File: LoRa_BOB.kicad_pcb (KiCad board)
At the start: 4 copper layers, 23 x 77 mm, 6 parts, among them U1 RFM95W-915S2

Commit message: Minor advances
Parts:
- removed the A1 at (174.2, 162.9)
- added C3: 0.1uF, Capacitor_SMD:C_0805_2012Metric_Pad1.18x1.45mm_HandSolder, F.Cu at (255.6, 172.8)
- added U1: XC6210B332MR-G, Package_TO_SOT_SMD:SOT-23-5, F.Cu at (261.1, 168.0)
- added U3: 74HC4050D, Package_SO:SOIC-16_3.9x9.9mm_P1.27mm, F.Cu at (255.7, 179.1)
- C1, C2: value C -> 10uF; footprint Capacitor_SMD:C_0805_2012Metric_Pad1.18x1.45mm_HandSolder -> Capacitor_SMD:C_1206_3216Metric_Pad1.33x1.80mm_HandSolder
- moved C1 40.6 mm to (264.7, 168.2)
- moved C2 36.3 mm to (255.6, 168.8)
- renumbered A2 to A1, U1 to U2
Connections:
- A1 pad 11: unconnected-(A2-SCK/D24-Pad11) -> /SCK
- A1 pad 12: unconnected-(A2-MOSI/D23-Pad12) -> /MOSI
- A1 pad 13: unconnected-(A2-MISO/D22-Pad13) -> /MISO
- A1 pad 16: unconnected-(A2-DIO1-Pad16) -> Net-(A1-DIO1)
- A1 pad 2: Net-(A2-3V3) -> Net-(A1-3V3)
- A1 pad 26: unconnected-(A2-USB-Pad26) -> Net-(A1-USB)
- A1 pad 6: unconnected-(A2-A1-Pad6) -> /~{RESET}
- A1 pad 7: Net-(A2-A2) -> /CS
- A1 pad 9: Net-(A2-A4) -> Net-(A1-A4)
- C1 pad 1: Net-(A2-3V3) -> Net-(A1-USB)
- C1 pad 2: GND -> Net-(U1-GND)
- C2 pad 1: Net-(A2-3V3) -> +3V3
- C2 pad 2: GND -> Net-(U1-GND)
- U2 pad 13: Net-(A2-3V3) -> +3V3
- U2 pad 15: unconnected-(U1-DIO1-Pad15) -> Net-(A1-DIO1)
- U2 pad 2: unconnected-(U1-MISO-Pad2) -> /MISO
- U2 pad 3: unconnected-(U1-MOSI-Pad3) -> /MOSI_3V
- U2 pad 4: unconnected-(U1-SCK-Pad4) -> /SCK_3V
- U2 pad 5: Net-(A2-A2) -> /CS_3V
- U2 pad 6: Net-(A2-A4) -> Net-(U2-RESET)

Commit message: Routed but could be better
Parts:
- moved C3 31.7 mm to (254.2, 204.5)
- moved AE1 2.56 mm to (257.2, 221.1)
- moved U1 2.07 mm to (259.1, 167.6)
- moved C2 2.01 mm to (254.0, 167.6)
- moved U3 2.00 mm to (257.1, 177.7)
- moved U2 1.41 mm to (256.6, 192.9)
- moved A1 1.19 mm to (246.4, 162.5)
- moved C1 0.76 mm to (264.2, 167.6)
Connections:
- A1 pad 2: Net-(A1-3V3) -> unconnected-(A1-3V3-Pad2)
- C1 pad 2: Net-(U1-GND) -> GND
- C2 pad 2: Net-(U1-GND) -> GND
- C3 pad 2: Net-(U1-GND) -> GND
- U1 pad 2: Net-(U1-GND) -> GND
- U3 pad 1: Net-(A1-3V3) -> +3V3
- U3 pad 8: unconnected-(U3-GND-Pad8) -> GND
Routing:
- net /MOSI: track 0.00 -> 23.6 mm, vias 0 -> 1
- net Net-(A1-A5): track 0.00 -> 20.8 mm
- net Net-(A1-USB): track 0.00 -> 20.6 mm, vias 0 -> 2
- net /CS_3V: track 0.00 -> 20.5 mm
- net Net-(A1-DIO1): track 0.00 -> 19.6 mm, vias 0 -> 2
- net /MISO: track 0.00 -> 19.2 mm, vias 0 -> 2
- net /SCK: track 0.00 -> 13.7 mm, vias 0 -> 1
- net +3V3: track 0.00 -> 13.6 mm, vias 0 -> 4
- net /CS: track 0.00 -> 12.9 mm
- net GND: track 0.00 -> 12.3 mm, vias 0 -> 5
- net /MOSI_3V: track 0.00 -> 10.9 mm, vias 0 -> 2
- net Net-(A1-A4): track 0.00 -> 7.42 mm
- net /SCK_3V: track 0.00 -> 5.64 mm, vias 0 -> 2
- net Net-(U2-RESET): track 0.00 -> 5.35 mm
- net Net-(AE1-A): track 11.7 -> 15.2 mm
- added copper zone on In2.Cu, net +3V3
- added copper zone on B.Cu, net GND
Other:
- board size 23 x 77 mm -> 22.9 x 77.5 mm

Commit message: New Template
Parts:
- removed A1: Adafruit_Feather_M0_RFM9x_LoRa_Radio, Module:Adafruit_Feather_M0_RFM
- removed AE1: Antenna, RF_Antenna:Texas_SWRA416_868MHz_915MHz
- removed C1, C2: 10uF, Capacitor_SMD:C_1206_3216Metric_Pad1.33x1.80mm_HandSolder
- removed C3: 0.1uF, Capacitor_SMD:C_0805_2012Metric_Pad1.18x1.45mm_HandSolder
- removed U1: XC6210B332MR-G, Package_TO_SOT_SMD:SOT-23-5
- removed U2: RFM95W-915S2, RF_Module:HOPERF_RFM9XW_SMD
- removed U3: 74HC4050D, Package_SO:SOIC-16_3.9x9.9mm_P1.27mm
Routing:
- net /MOSI: track 23.6 -> 0.00 mm, vias 1 -> 0
- net Net-(A1-A5): track 20.8 -> 0.00 mm
- net Net-(A1-USB): track 20.6 -> 0.00 mm, vias 2 -> 0
- net /CS_3V: track 20.5 -> 0.00 mm
- net Net-(A1-DIO1): track 19.6 -> 0.00 mm, vias 2 -> 0
- net /MISO: track 19.2 -> 0.00 mm, vias 2 -> 0
- net Net-(AE1-A): track 15.2 -> 0.00 mm
- net /SCK: track 13.7 -> 0.00 mm, vias 1 -> 0
- net +3V3: track 13.6 -> 0.00 mm, vias 4 -> 0
- net /CS: track 12.9 -> 0.00 mm
- net GND: track 12.3 -> 0.00 mm, vias 5 -> 0
- net /MOSI_3V: track 10.9 -> 0.00 mm, vias 2 -> 0
- net Net-(A1-A4): track 7.42 -> 0.00 mm
- net /SCK_3V: track 5.64 -> 0.00 mm, vias 2 -> 0
- net Net-(U2-RESET): track 5.35 -> 0.00 mm
- removed copper zone on In2.Cu, net +3V3
- removed copper zone on B.Cu, net GND
- removed copper zone on In1.Cu, net GND
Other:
- board outline removed

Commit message: basic, with trick Feather and RFM
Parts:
- added A1: Adafruit_Feather_M0_RFM9x_LoRa_Radio, Module:Adafruit_Feather_M0_RFM, F.Cu at (198.9, 108.3)
- added C1: 10uF, Capacitor_SMD:C_1206_3216Metric_Pad1.33x1.80mm_HandSolder, F.Cu at (210.8, 111.2)
- added C2: 10uF, Capacitor_SMD:C_1206_3216Metric_Pad1.33x1.80mm_HandSolder, F.Cu at (216.1, 109.0)
- added C3: 0.1uF, Capacitor_SMD:C_0805_2012Metric_Pad1.18x1.45mm_HandSolder, F.Cu at (206.5, 151.3)
- added U1: RFM97W-915S2, RF_Module:HOPERF_RFM9XW_SMD, F.Cu at (209.0, 139.9)
- added U2: XC6210B332MR-G, Package_TO_SOT_SMD:SOT-23-5, F.Cu at (216.3, 113.7)
- added U3: 74HC4050D, Package_SO:SOIC-16_3.9x9.9mm_P1.27mm, F.Cu at (209.2, 125.0)

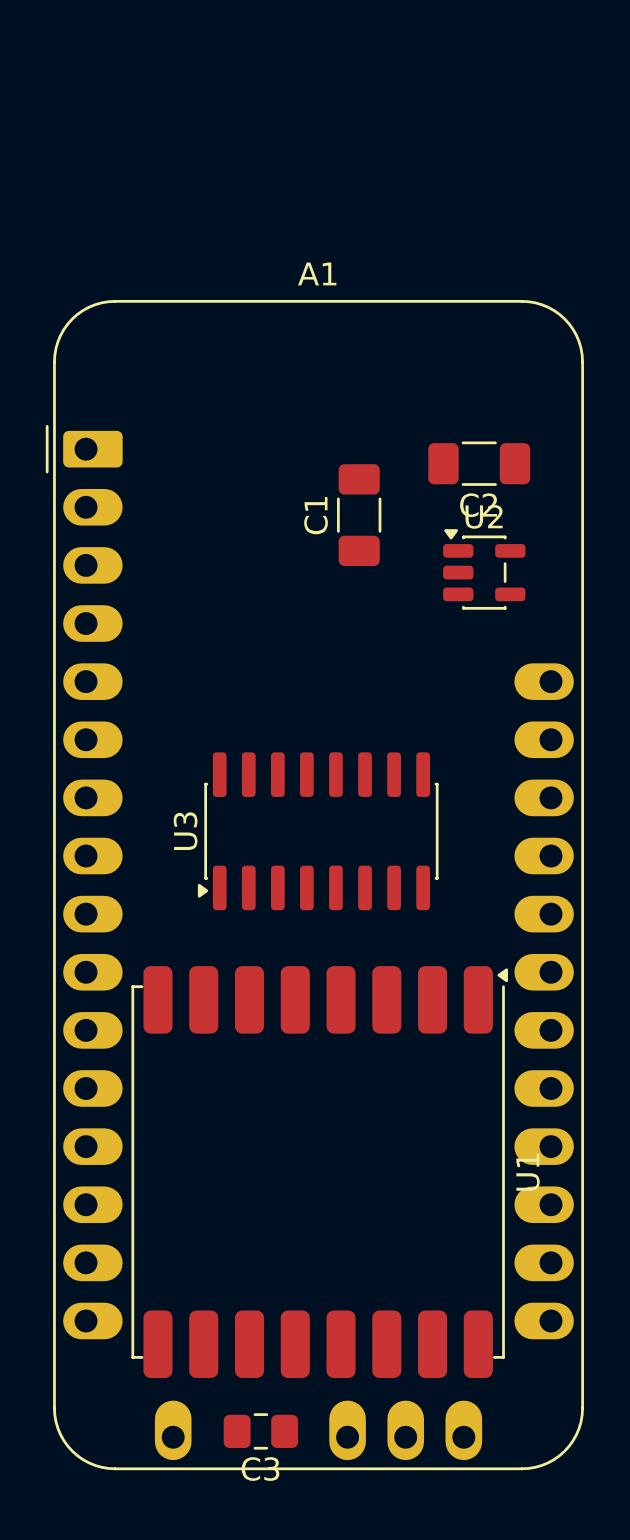
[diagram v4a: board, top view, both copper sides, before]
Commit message: edited existing footprints and symbol
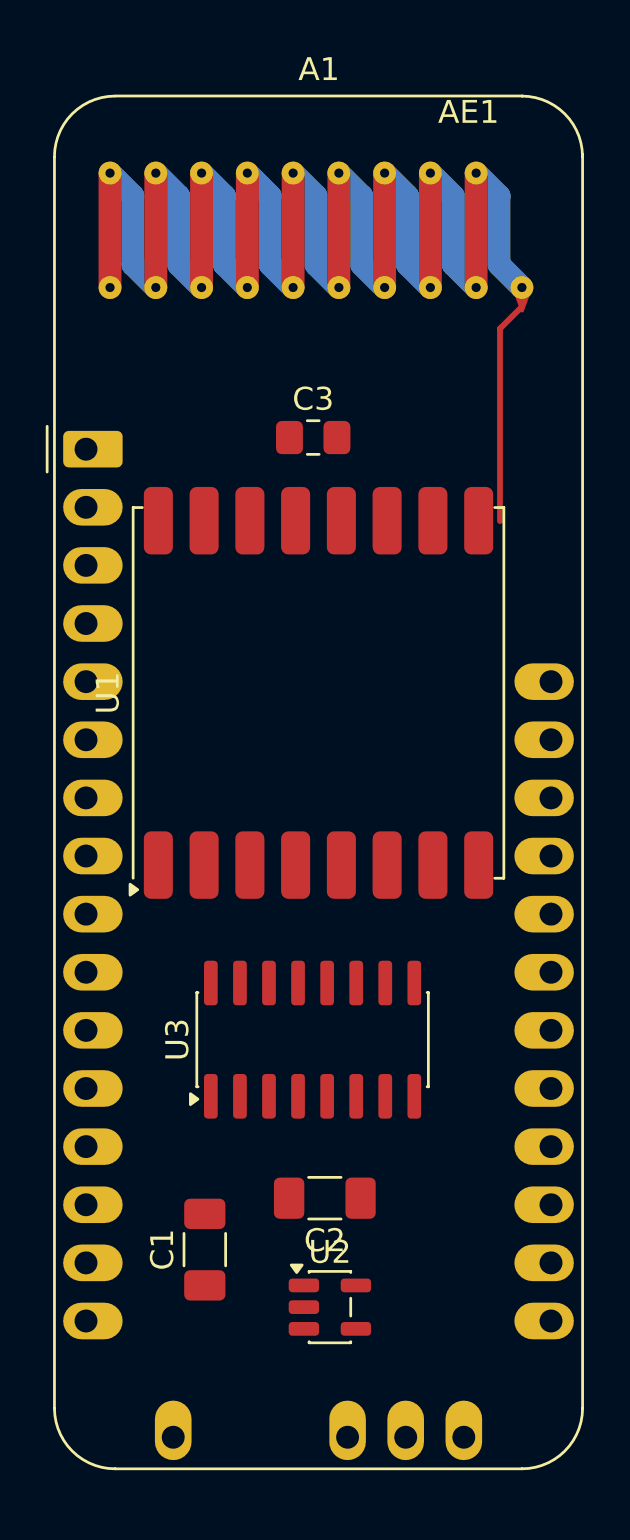
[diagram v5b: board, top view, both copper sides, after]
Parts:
- added AE1: Antenna, RF_Antenna:Texas_SWRA416_868MHz_915MHz, F.Cu at (208.9, 95.5)
- A1: value Adafruit_Feather_M0_RFM9x_LoRa_Radio -> Adafruit_Feather_RFM9x_LoRa_Radio
- U1: value RFM97W-915S2 -> 1597-1488-ND
- moved C3 43.5 mm to (208.8, 107.8), turned to 0 degrees
- moved U2 32.8 mm to (209.5, 145.8)
- moved C1 32.8 mm to (204.1, 143.3)
- moved C2 32.8 mm to (209.3, 141.1)
- moved U1 20.9 mm to (209.0, 119.0), turned to 90 degrees
- moved U3 9.11 mm to (208.8, 134.1)
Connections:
- U1 pad 9: unconnected-(U1-ANT-Pad9) -> Net-(AE1-A)
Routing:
- net Net-(AE1-A): track 0.00 -> 9.78 mm

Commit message: pours
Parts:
- moved U3 1.28 mm to (210.1, 134.1), turned to -90 degrees
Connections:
- A1 pad 11: unconnected-(A1-SCK/D24-Pad11) -> /SCK
- A1 pad 12: unconnected-(A1-MOSI/D23-Pad12) -> /MOSI
- A1 pad 13: unconnected-(A1-MISO/D22-Pad13) -> /MISO
- A1 pad 29: unconnected-(A1-ANT-Pad29) -> (no net)
- A1 pad 4: unconnected-(A1-GND-Pad4) -> GND
- U1 pad 2: unconnected-(U1-MISO-Pad2) -> /MISO
- U1 pad 6: unconnected-(U1-RESET-Pad6) -> /~{RESET_3V}
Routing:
- added copper zone on In2.Cu, net +3V3
- added copper zone on B.Cu, net GND
- added copper zone on F.Cu, net GND
- added copper zone on In1.Cu, net GND
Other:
- board outline added: 22.9 x 59.7 mm

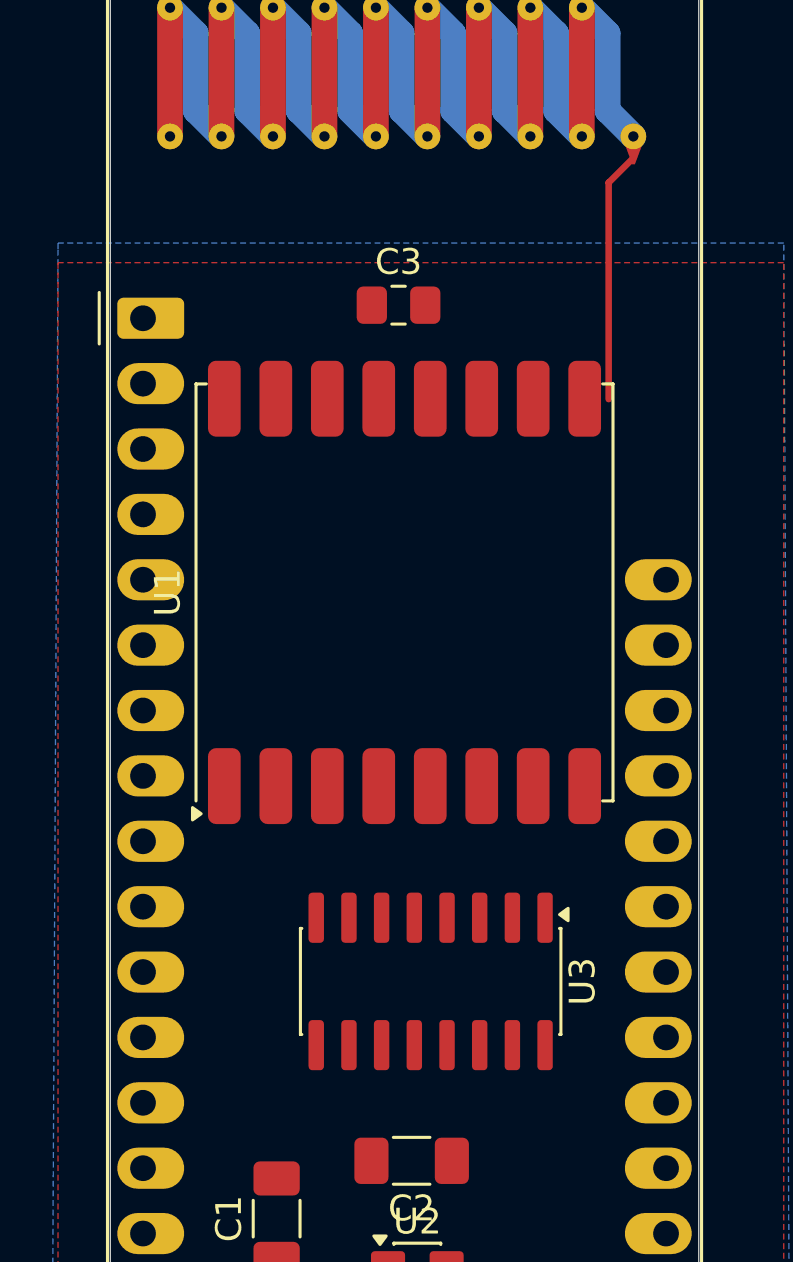
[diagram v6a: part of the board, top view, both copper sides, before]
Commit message: netclass routing
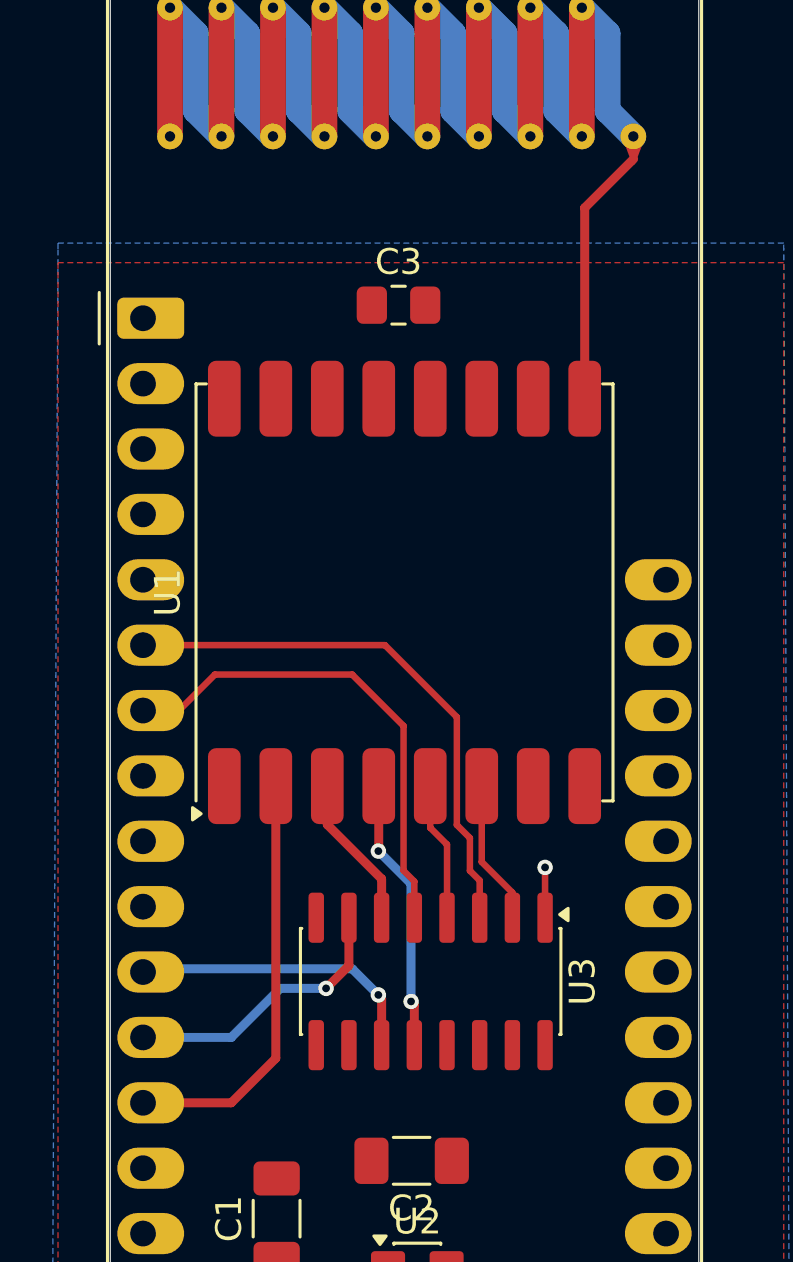
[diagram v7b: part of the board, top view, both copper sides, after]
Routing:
- net /~{RESET}: track 0.00 -> 22.1 mm
- net /CS: track 0.00 -> 19.2 mm
- net /MISO: track 0.00 -> 16.4 mm
- net /SCK: track 0.00 -> 11.6 mm, vias 0 -> 1
- net /MOSI: track 0.00 -> 11.0 mm, vias 0 -> 1
- net /SCK_3V: track 0.00 -> 10.6 mm, vias 0 -> 2
- net /MOSI_3V: track 0.00 -> 5.99 mm
- net /~{RESET_3V}: track 0.00 -> 5.61 mm
- net /CS_3V: track 0.00 -> 5.38 mm
- net +3V3: track 0.00 -> 2.13 mm, vias 0 -> 1

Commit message: better routing
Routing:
- net Net-(A1-DIO1): track 0.00 -> 61.4 mm, vias 0 -> 1
- net Net-(A1-USB): track 0.00 -> 36.6 mm, vias 0 -> 1
- net Net-(A1-A5): track 0.00 -> 23.4 mm, vias 0 -> 1
- net +3V3: track 2.13 -> 14.5 mm, vias 1 -> 5
- net /MISO: track 16.4 -> 15.3 mm
- net GND: vias 0 -> 13
